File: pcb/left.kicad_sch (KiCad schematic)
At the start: 72 parts, among them SW1 TAB, SW10 D, SW11 F, SW12 G, SW13 CTRL, SW14 Z, SW15 X, SW16 C, SW17 V, SW18 B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

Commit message: Wire left half of pcb
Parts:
- added J1: AudioJack3, audio-jacks:PJ-399B-6A, symbol Connector_Audio:AudioJack3
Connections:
- net ENCODER1_CLK: now also U1.31 (GPIO26_ADC0)
- net ENCODER1_DT: now also U1.22 (GPIO17)
- net ENCODER1_SW: now also U1.32 (GPIO27_ADC1)
- net ENCODER2_CLK: now also U1.17 (GPIO13)
- net ENCODER2_DT: now also U1.19 (GPIO14)
- net ENCODER2_SW: now also U1.20 (GPIO15); no longer U1.29 (GPIO22)
- net GND: now also U1.13 (GND), U1.18 (GND), U1.23 (GND), U1.28 (GND), U1.3 (GND), U1.38 (GND), U1.8 (GND), J1.S; no longer U1.33 (AGND)
- net UART0_TX: now reaches U1.1 (GPIO0)
- net UART0_TX: now also J1.R
- net UART0_RX: now reaches U1.2 (GPIO1)
- net UART0_RX: now also J1.T
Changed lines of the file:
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@@
 	(wire
 		(pts
+			(xy 81.28 104.14) (xy 82.55 104.14)
+		)
+		(stroke
+			(width 0)
+			(type default)
+		)
+	)
+	(wire
+		(pts
 			(xy 44.45 138.43) (xy 45.72 138.43)
 		)
@@
 	(wire
 		(pts
+			(xy 21.59 76.2) (xy 22.86 76.2)
+		)
+		(stroke
+			(width 0)
+			(type default)
+		)
+	)
+	(wire
+		(pts
 			(xy 60.96 124.46) (xy 62.23 124.46)
 		)
@@
 	(wire
 		(pts
+			(xy 45.72 99.06) (xy 45.72 100.33)
+		)
+		(stroke
+			(width 0)
+			(type default)
+		)
+	)
+	(wire
+		(pts
 			(xy 191.77 116.84) (xy 199.39 116.84)
 		)
@@
 	(wire
 		(pts
+			(xy 21.59 73.66) (xy 22.86 73.66)
+		)
+		(stroke
+			(width 0)
+			(type default)
+		)
+	)
+	(wire
+		(pts
 			(xy 229.87 129.54) (xy 236.22 129.54)
 		)
@@
 	(wire
 		(pts
+			(xy 81.28 101.6) (xy 82.55 101.6)
+		)
+		(stroke
+			(width 0)
+			(type default)
+		)
+	)
+	(wire
+		(pts
 			(xy 115.57 22.86) (xy 115.57 25.4)
 		)
@@
 	(wire
 		(pts
-			(xy 68.58 60.96) (xy 69.85 60.96)
+			(xy 68.58 71.12) (xy 69.85 71.12)
 		)
 		(stroke
@@
 	(wire
 		(pts
-			(xy 68.58 81.28) (xy 71.12 81.28)
-		)
-		(stroke
-			(width 0)
-			(type default)
-		)
-	)
-	(wire
-		(pts
 			(xy 40.64 140.97) (xy 45.72 140.97)
 		)
@@
 	(wire
 		(pts
+			(xy 68.58 73.66) (xy 69.85 73.66)
+		)
+		(stroke
+			(width 0)
+			(type default)
+		)
+	)
+	(wire
+		(pts
 			(xy 153.67 99.06) (xy 153.67 101.6)
 		)
@@
 	(wire
 		(pts
+			(xy 21.59 71.12) (xy 22.86 71.12)
+		)
+		(stroke
+			(width 0)
+			(type default)
+		)
+	)
+	(wire
+		(pts
 			(xy 243.84 139.7) (xy 243.84 137.16)
 		)
@@
 	(wire
 		(pts
+			(xy 21.59 38.1) (xy 22.86 38.1)
+		)
+		(stroke
+			(width 0)
+			(type default)
+		)
+	)
+	(wire
+		(pts
 			(xy 199.39 71.12) (xy 222.25 71.12)
 		)
@@
 	(wire
 		(pts
+			(xy 21.59 40.64) (xy 22.86 40.64)
+		)
+		(stroke
+			(width 0)
+			(type default)
+		)
+	)
+	(wire
+		(pts
 			(xy 245.11 144.78) (xy 243.84 144.78)
 		)
@@
 	(wire
 		(pts
+			(xy 81.28 106.68) (xy 82.55 106.68)
+		)
+		(stroke
+			(width 0)
+			(type default)
+		)
+	)
+	(wire
+		(pts
+			(xy 68.58 48.26) (xy 69.85 48.26)
+		)
+		(stroke
+			(width 0)
+			(type default)
+		)
+	)
+	(wire
+		(pts
 			(xy 44.45 119.38) (xy 45.72 119.38)
 		)
@@
 	)
 	(label "ENCODER1_SW"
-		(at 71.12 67.31 0)
+		(at 69.85 73.66 0)
 		(fields_autoplaced yes)
 		(effects
@@
 	)
 	(label "ENCODER2_CLK"
-		(at 71.12 72.39 0)
+		(at 21.59 71.12 180)
 		(fields_autoplaced yes)
 		(effects
@@
 				(size 1.27 1.27)
 			)
-			(justify left bottom)
+			(justify right bottom)
 		)
 	)
@@
 		)
 	)
+	(label "UART0_RX"
+		(at 21.59 40.64 180)
+		(fields_autoplaced yes)
+		(effects
+			(font
+				(size 1.27 1.27)
+			)
+			(justify right bottom)
+		)
+	)
 	(label "GND"
 		(at 191.77 116.84 0)
@@
 		)
 	)
+	(label "UART0_TX"
+		(at 82.55 104.14 0)
+		(fields_autoplaced yes)
+		(effects
+			(font
+				(size 1.27 1.27)
+			)
+			(justify left bottom)
+		)
+	)
 	(label "ENCODER1_DT"
 		(at 44.45 143.51 180)
@@
 	)
 	(label "ENCODER1_CLK"
-		(at 67.31 86.36 0)
+		(at 69.85 71.12 0)
 		(fields_autoplaced yes)
 		(effects
@@
 		)
 	)
+	(label "UART0_RX"
+		(at 82.55 106.68 0)
+		(fields_autoplaced yes)
+		(effects
+			(font
+				(size 1.27 1.27)
+			)
+			(justify left bottom)
+		)
+	)
 	(label "GND"
 		(at 191.77 162.56 0)
@@
 	)
 	(label "ENCODER1_DT"
-		(at 67.31 88.9 0)
+		(at 69.85 48.26 0)
 		(fields_autoplaced yes)
 		(effects
@@
 		)
 	)
+	(label "GND"
+		(at 82.55 101.6 0)
+		(fields_autoplaced yes)
+		(effects
+			(font
+				(size 1.27 1.27)
+			)
+			(justify left bottom)
+		)
+	)
+	(label "UART0_TX"
+		(at 21.59 38.1 180)
+		(fields_autoplaced yes)
+		(effects
+			(font
+				(size 1.27 1.27)
+			)
+			(justify right bottom)
+		)
+	)
 	(label "5v"
 		(at 245.11 99.06 0)
@@
 	)
 	(label "ENCODER2_SW"
-		(at 69.85 60.96 0)
+		(at 21.59 76.2 180)
 		(fields_autoplaced yes)
 		(effects
@@
 				(size 1.27 1.27)
 			)
-			(justify left bottom)
+			(justify right bottom)
 		)
 	)
 	(label "GND"
-		(at 71.12 81.28 0)
+		(at 45.72 100.33 270)
 		(fields_autoplaced yes)
 		(effects
@@
 				(size 1.27 1.27)
 			)
-			(justify left bottom)
+			(justify right bottom)
 		)
 	)
@@
 	)
 	(label "ENCODER2_DT"
-		(at 71.12 74.93 0)
+		(at 21.59 73.66 180)
 		(fields_autoplaced yes)
 		(effects
@@
 				(size 1.27 1.27)
 			)
-			(justify left bottom)
+			(justify right bottom)
 		)
 	)
@@
 					(unit 1)
 				)
+			)
+		)
+	)
+	(symbol
+		(lib_id "Connector_Audio:AudioJack3")
+		(at 76.2 104.14 0)
+		(unit 1)
+		(exclude_from_sim no)
+		(in_bom yes)
+		(on_board yes)
+		(dnp no)
+		(fields_autoplaced yes)
+		(property "Reference" "J1"
+			(at 74.295 95.25 0)
+			(effects
+				(font
+					(size 1.27 1.27)
+				)
+			)
+		)
+		(property "Value" "AudioJack3"
+			(at 74.295 97.79 0)
+			(effects
+				(font
+					(size 1.27 1.27)
+				)
+			)
+		)
+		(property "Footprint" "audio-jacks:PJ-399B-6A"
+			(at 76.2 104.14 0)
+			(effects
+				(font
+					(size 1.27 1.27)
+				)
+				(hide yes)
+			)
+		)
+		(property "Datasheet" "~"
+			(at 76.2 104.14 0)
+			(effects
+				(font
+					(size 1.27 1.27)
+				)
+				(hide yes)
+			)
+		)
+		(property "Description" "Audio Jack, 3 Poles (Stereo / TRS)"
+			(at 76.2 104.14 0)
+			(effects
+				(font
+					(size 1.27 1.27)
+				)
+				(hide yes)
+			)
+		)
+		(pin "S"
+		)
+		(pin "R"
+		)
+		(pin "T"
+		)
+		(instances
+			(project ""
+				(path "/f40e124c-e4be-4508-9534-c431f9be00da/d4dd398f-8031-42f5-9517-3577efda2268"
+					(reference "J1")
+					(unit 1)
+				)

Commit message: Rewire left half
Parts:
- SW45: value T -> EX1
- SW46: value G -> EX2
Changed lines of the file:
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@@
 			)
 		)
-		(property "Value" "T"
+		(property "Value" "EX1"
 			(at 173.99 20.32 0)
 			(effects
@@
 			)
 		)
-		(property "Value" "G"
+		(property "Value" "EX2"
 			(at 173.99 45.72 0)
 			(effects

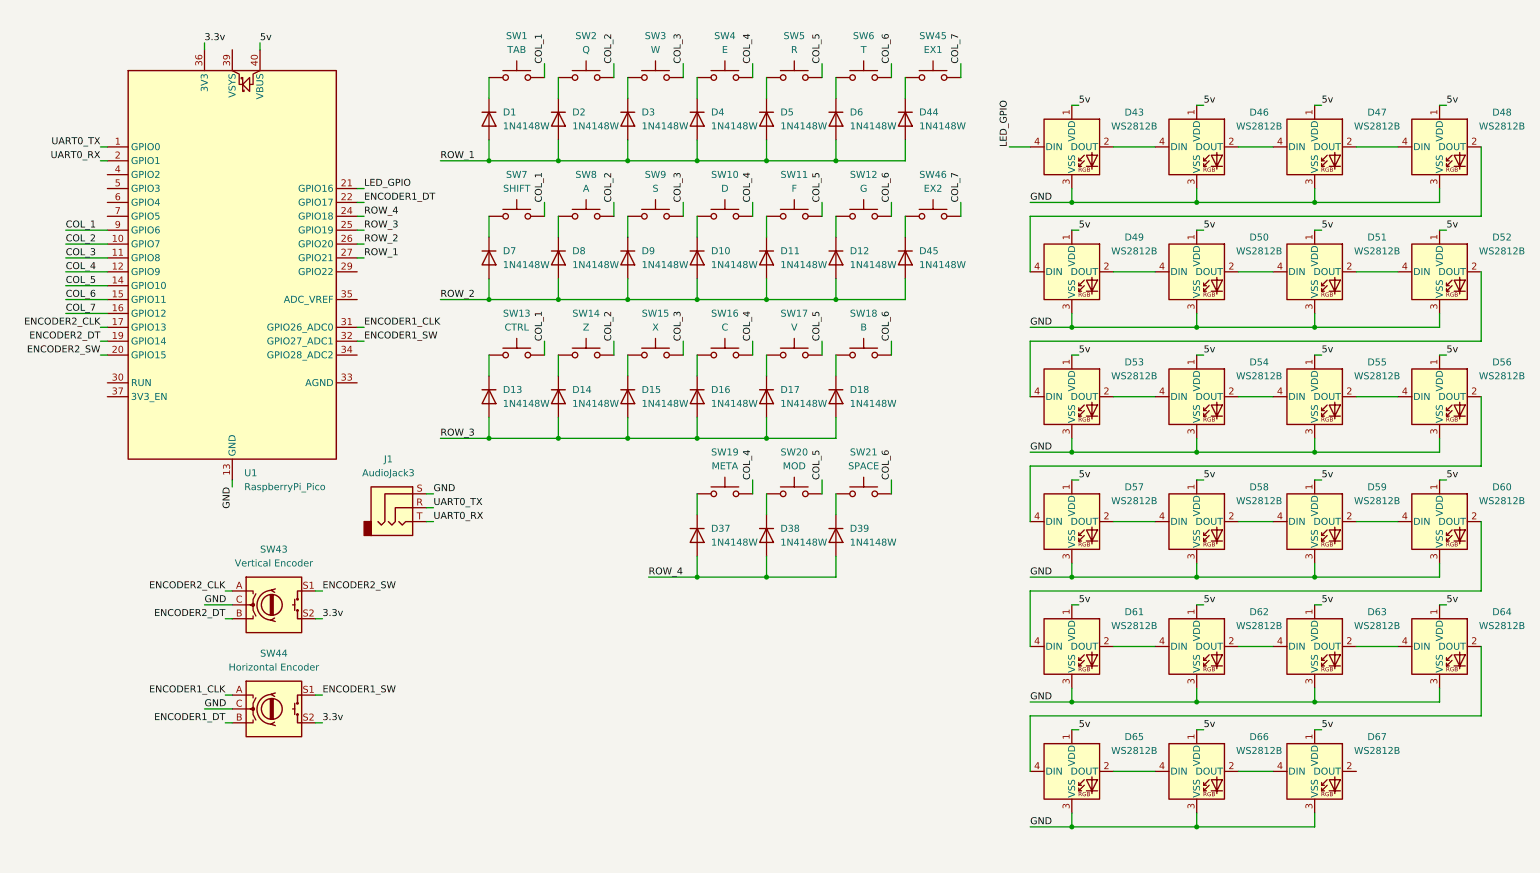
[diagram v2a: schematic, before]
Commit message: Move row and column to start with 0 on schematic
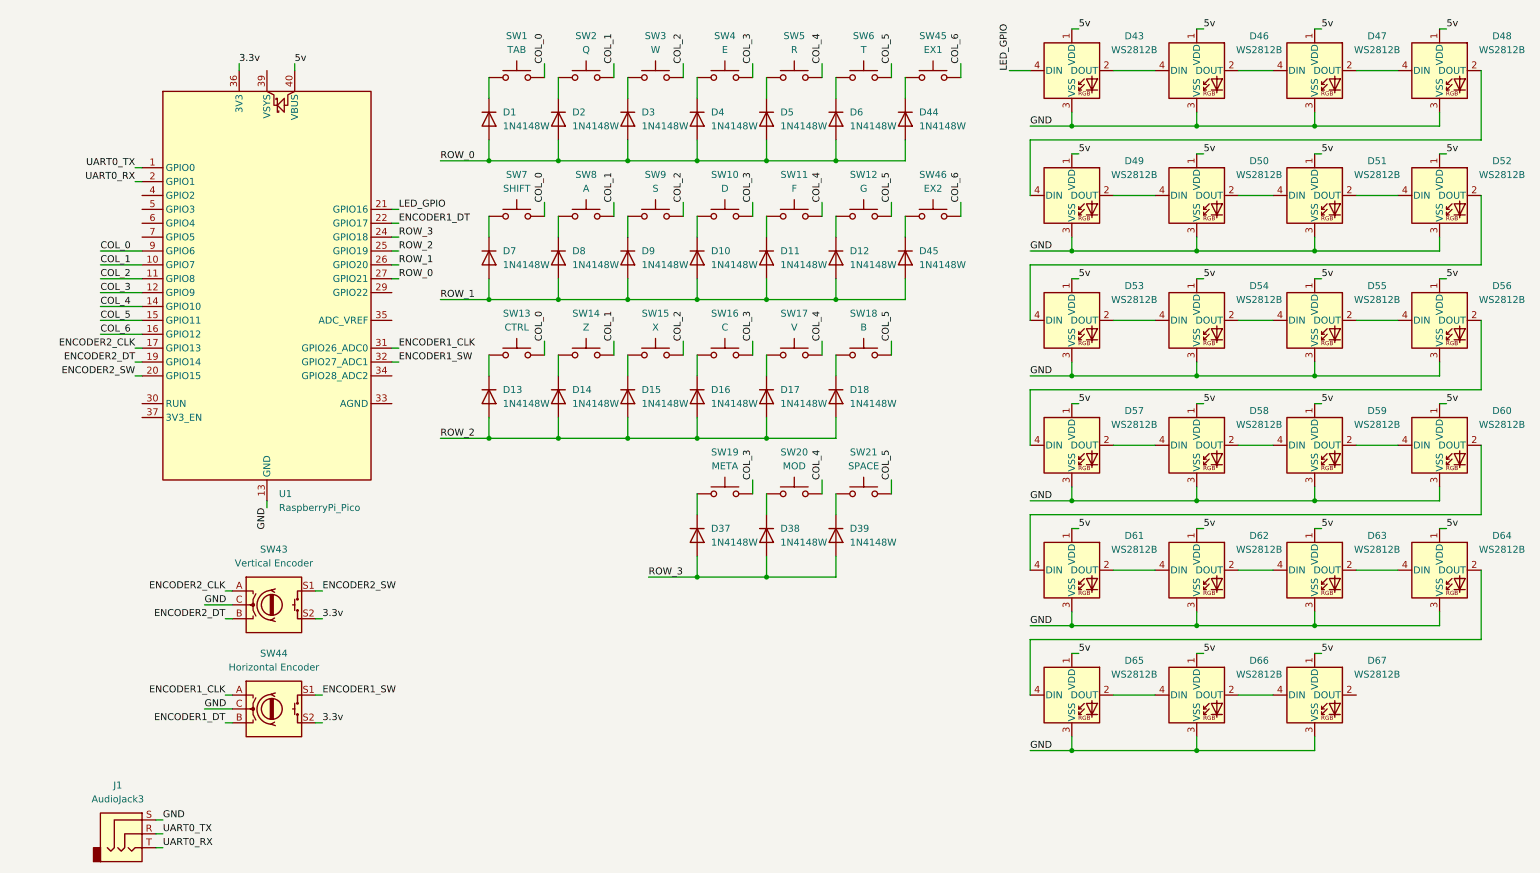
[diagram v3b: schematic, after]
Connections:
- net COL_7 is gone; now on net COL_6: SW45.2, SW46.2, U1.16 (GPIO12)
- net ROW_4 is gone; now on net ROW_3: D37.2 (A), D38.2 (A), D39.2 (A), U1.24 (GPIO18)
- net COL_1: now also SW14.2, SW2.2, SW8.2, U1.10 (GPIO7); no longer SW1.2, SW13.2, SW7.2, U1.9 (GPIO6)
- net COL_2: now also SW15.2, SW3.2, SW9.2, U1.11 (GPIO8); no longer SW14.2, SW2.2, SW8.2, U1.10 (GPIO7)
- net COL_3: now also SW10.2, SW16.2, SW19.2, SW4.2, U1.12 (GPIO9); no longer SW15.2, SW3.2, SW9.2, U1.11 (GPIO8)
- net COL_4: now also SW11.2, SW17.2, SW20.2, SW5.2, U1.14 (GPIO10); no longer SW10.2, SW16.2, SW19.2, SW4.2, U1.12 (GPIO9)
- net COL_5: now also SW12.2, SW18.2, SW21.2, SW6.2, U1.15 (GPIO11); no longer SW11.2, SW17.2, SW20.2, SW5.2, U1.14 (GPIO10)
- net COL_6: no longer SW12.2, SW18.2, SW21.2, SW6.2, U1.15 (GPIO11)
- net ROW_1: now also D10.2 (A), D11.2 (A), D12.2 (A), D45.2 (A), D7.2 (A), D8.2 (A), D9.2 (A), U1.26 (GPIO20); no longer D1.2 (A), D2.2 (A), D3.2 (A), D4.2 (A), D44.2 (A), D5.2 (A), D6.2 (A), U1.27 (GPIO21)
- net ROW_2: now also D13.2 (A), D14.2 (A), D15.2 (A), D16.2 (A), D17.2 (A), D18.2 (A), U1.25 (GPIO19); no longer D10.2 (A), D11.2 (A), D12.2 (A), D45.2 (A), D7.2 (A), D8.2 (A), D9.2 (A), U1.26 (GPIO20)
- net ROW_3: no longer D13.2 (A), D14.2 (A), D15.2 (A), D16.2 (A), D17.2 (A), D18.2 (A), U1.25 (GPIO19)
- new net COL_0: SW1.2, SW13.2, SW7.2, U1.9 (GPIO6)
- new net ROW_0: D1.2 (A), D2.2 (A), D3.2 (A), D4.2 (A), D44.2 (A), D5.2 (A), D6.2 (A), U1.27 (GPIO21)
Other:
- moved on the sheet: D43, D46, D47, D48, D49, D50, D51, D52, D53, D54, D55, D56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

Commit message: Switch to RP2040 chip on board
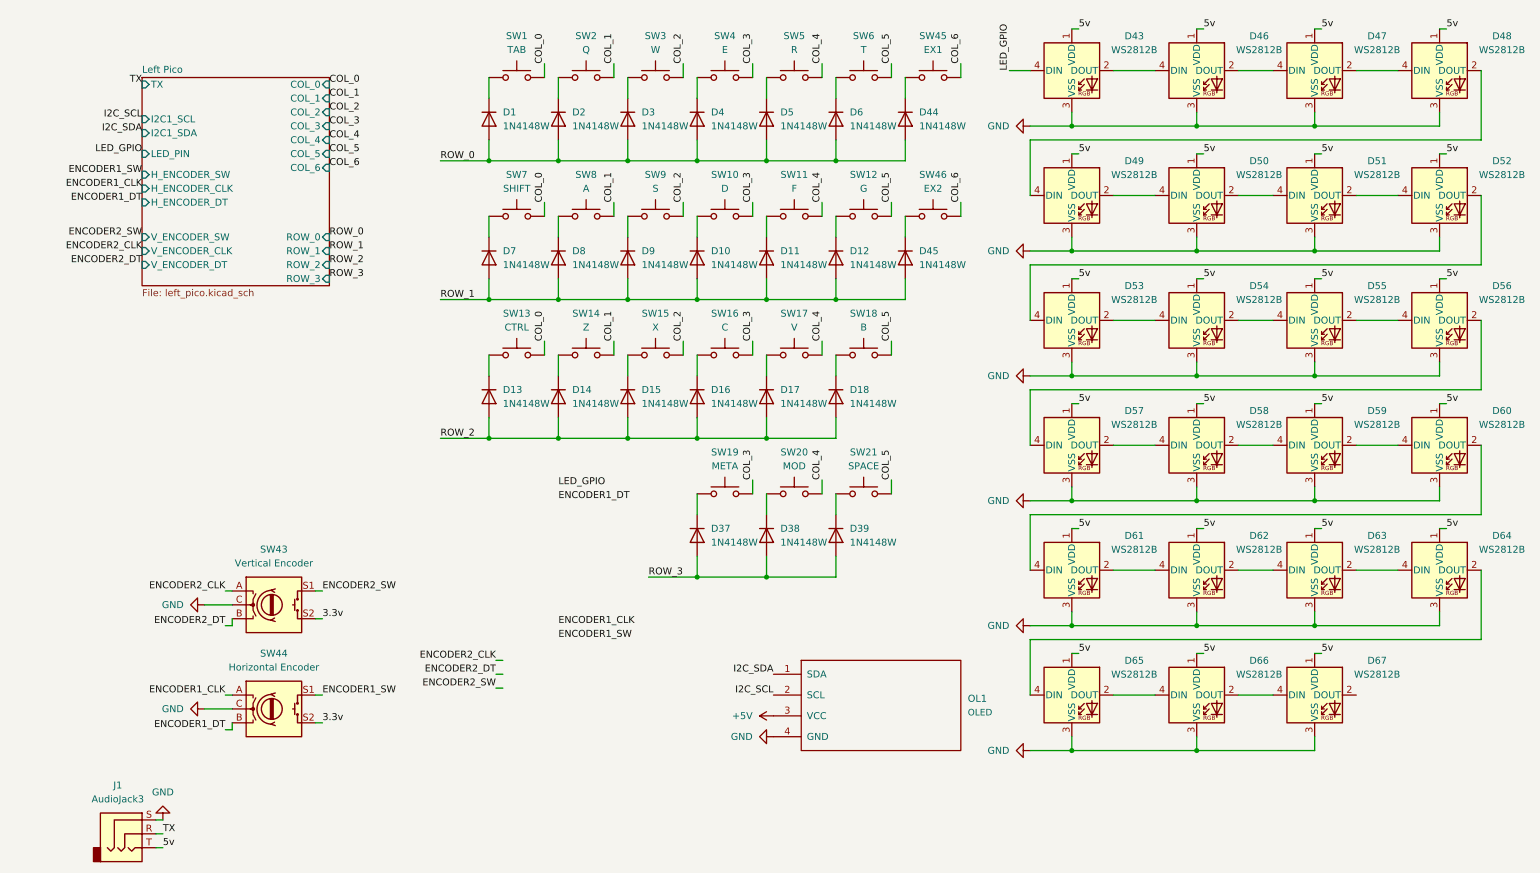
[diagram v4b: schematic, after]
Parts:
- removed U1: RaspberryPi_Pico, Module_RaspberryPi_Pico:RaspberryPi_Pico_Common, symbol MCU_Module_RaspberryPi_Pico:RaspberryPi_Pico
- added OL1: OLED, oled:SSD1306-0.91-OLED-4pin-128x32, symbol kbd:OLED
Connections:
- net UART0_RX is gone; now on net 5v: J1.T
- net GND: now also OL1.4 (GND)
- net UART0_TX renamed TX
- new net +5V: OL1.3 (VCC)
- new net I2C_SCL: OL1.2 (SCL)
- new net I2C_SDA: OL1.1 (SDA)
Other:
- added sheet Left Pico (left_pico.kicad_sch)
